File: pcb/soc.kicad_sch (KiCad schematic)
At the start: 1 part, among them U1 XC7Z020CLG484

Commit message: hierarchy and cleaning
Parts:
- removed U1: XC7Z020CLG484, Package_BGA:Xilinx_CLG484_CLG485, symbol library:XC7Z020CLG484
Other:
- added sheet FPGA 0, 13, 33 (soc-1.kicad_sch)
- added sheet FPGA 34, 35 (soc-2.kicad_sch)
- added sheet SoC DDR (soc-ddr.kicad_sch)
- added sheet SoC banks 500, 501 (soc-ps.kicad_sch)
- sheet Power ports: added 1V0_FD, 1V8_FD; removed none

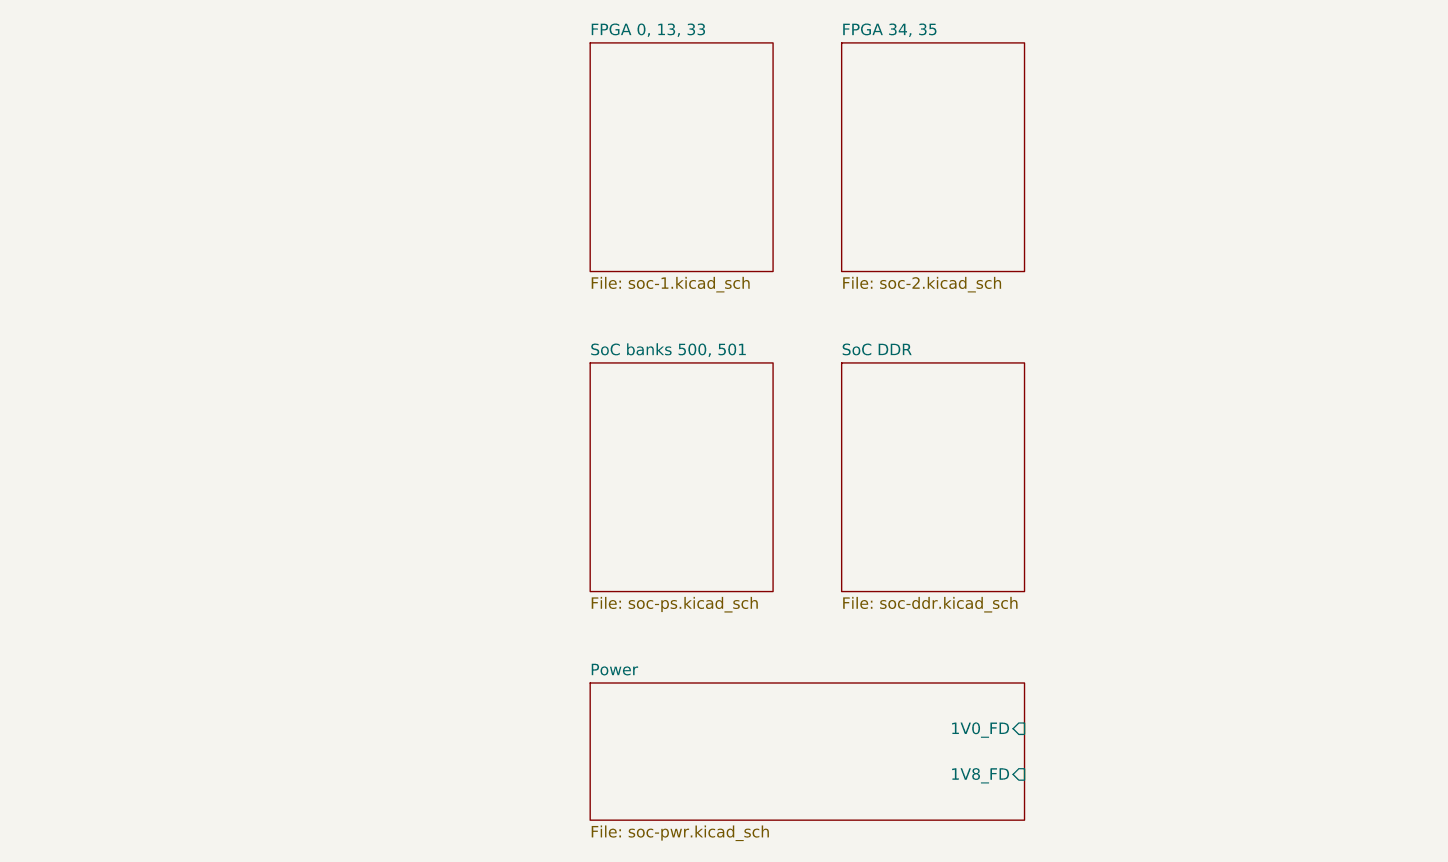
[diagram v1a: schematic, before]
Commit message: schematic structure, added qspi flash, pinout defs. mostly work on PS pinouts, defining comms. buses, still need to choose dram part, phys, camera/bus, power supply etc
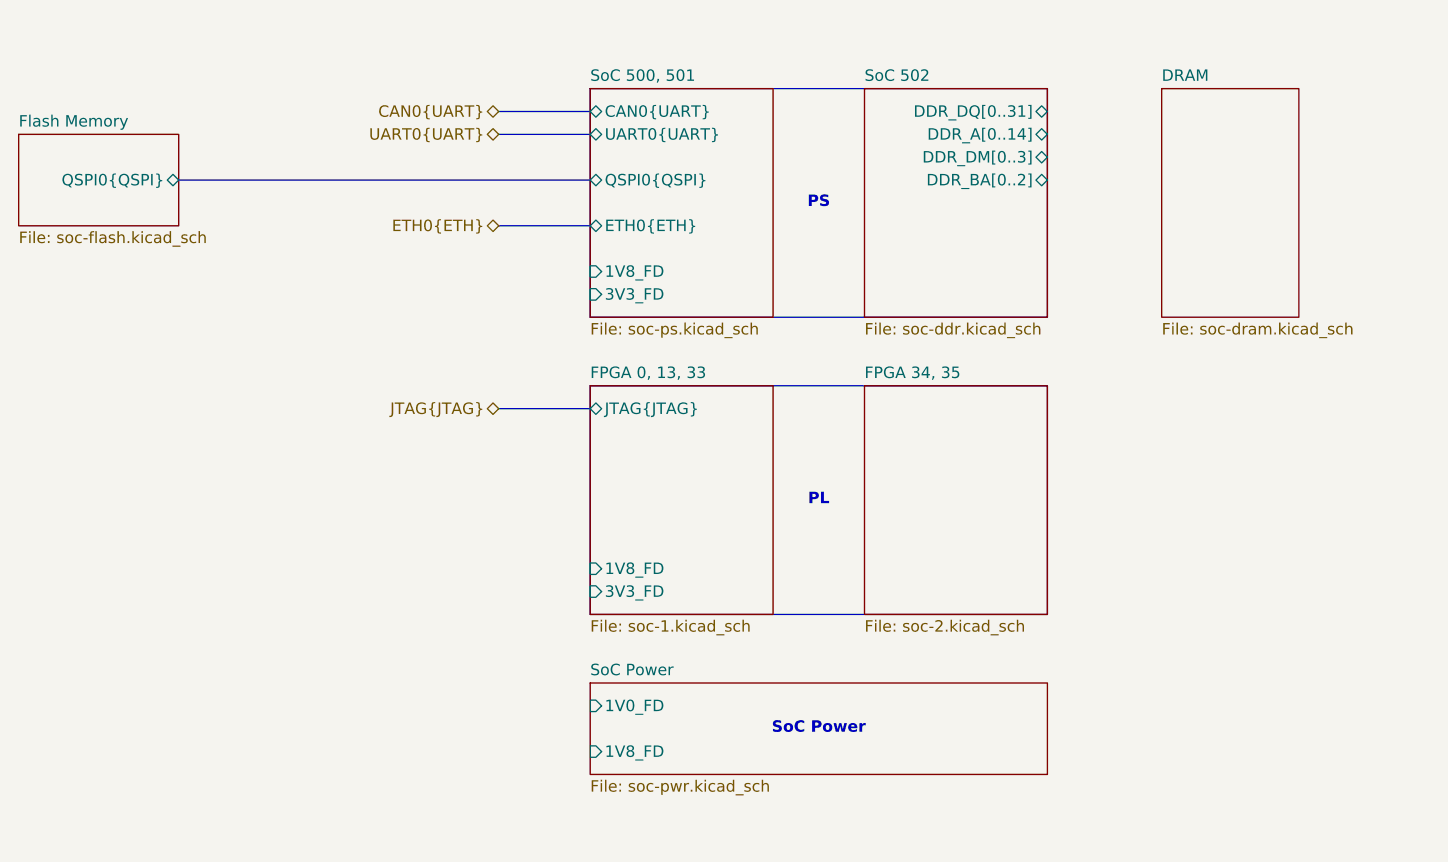
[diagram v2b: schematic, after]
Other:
- sheet Power renamed SoC Power
- sheet SoC DDR renamed SoC 502
- sheet SoC banks 500, 501 renamed SoC 500, 501
- added sheet DRAM (soc-dram.kicad_sch)
- added sheet Flash Memory (soc-flash.kicad_sch)
- sheet FPGA 0, 13, 33 ports: added 1V8_FD, 3V3_FD, JTAG{JTAG}; removed none
- sheet SoC 500, 501 ports: added 1V8_FD, 3V3_FD, CAN0{UART}, ETH0{ETH}, QSPI0{QSPI}, UART0{UART}; removed none
- sheet SoC 502 ports: added DDR_A[0..14], DDR_BA[0..2], DDR_DM[0..3], DDR_DQ[0..31]; removed none
- note added: "PL"
- note added: "PS"
- note added: "SoC Power"
- title: (none) -> CUTIE-CITRUS

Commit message: edits to eth0 protocol names / bus aliases
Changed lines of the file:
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@@
 		)
 	)
-	(hierarchical_label "ETH0{ETH}"
+	(hierarchical_label "ETH0{RGMII}"
 		(shape bidirectional)
 		(at 111.76 76.2 180)

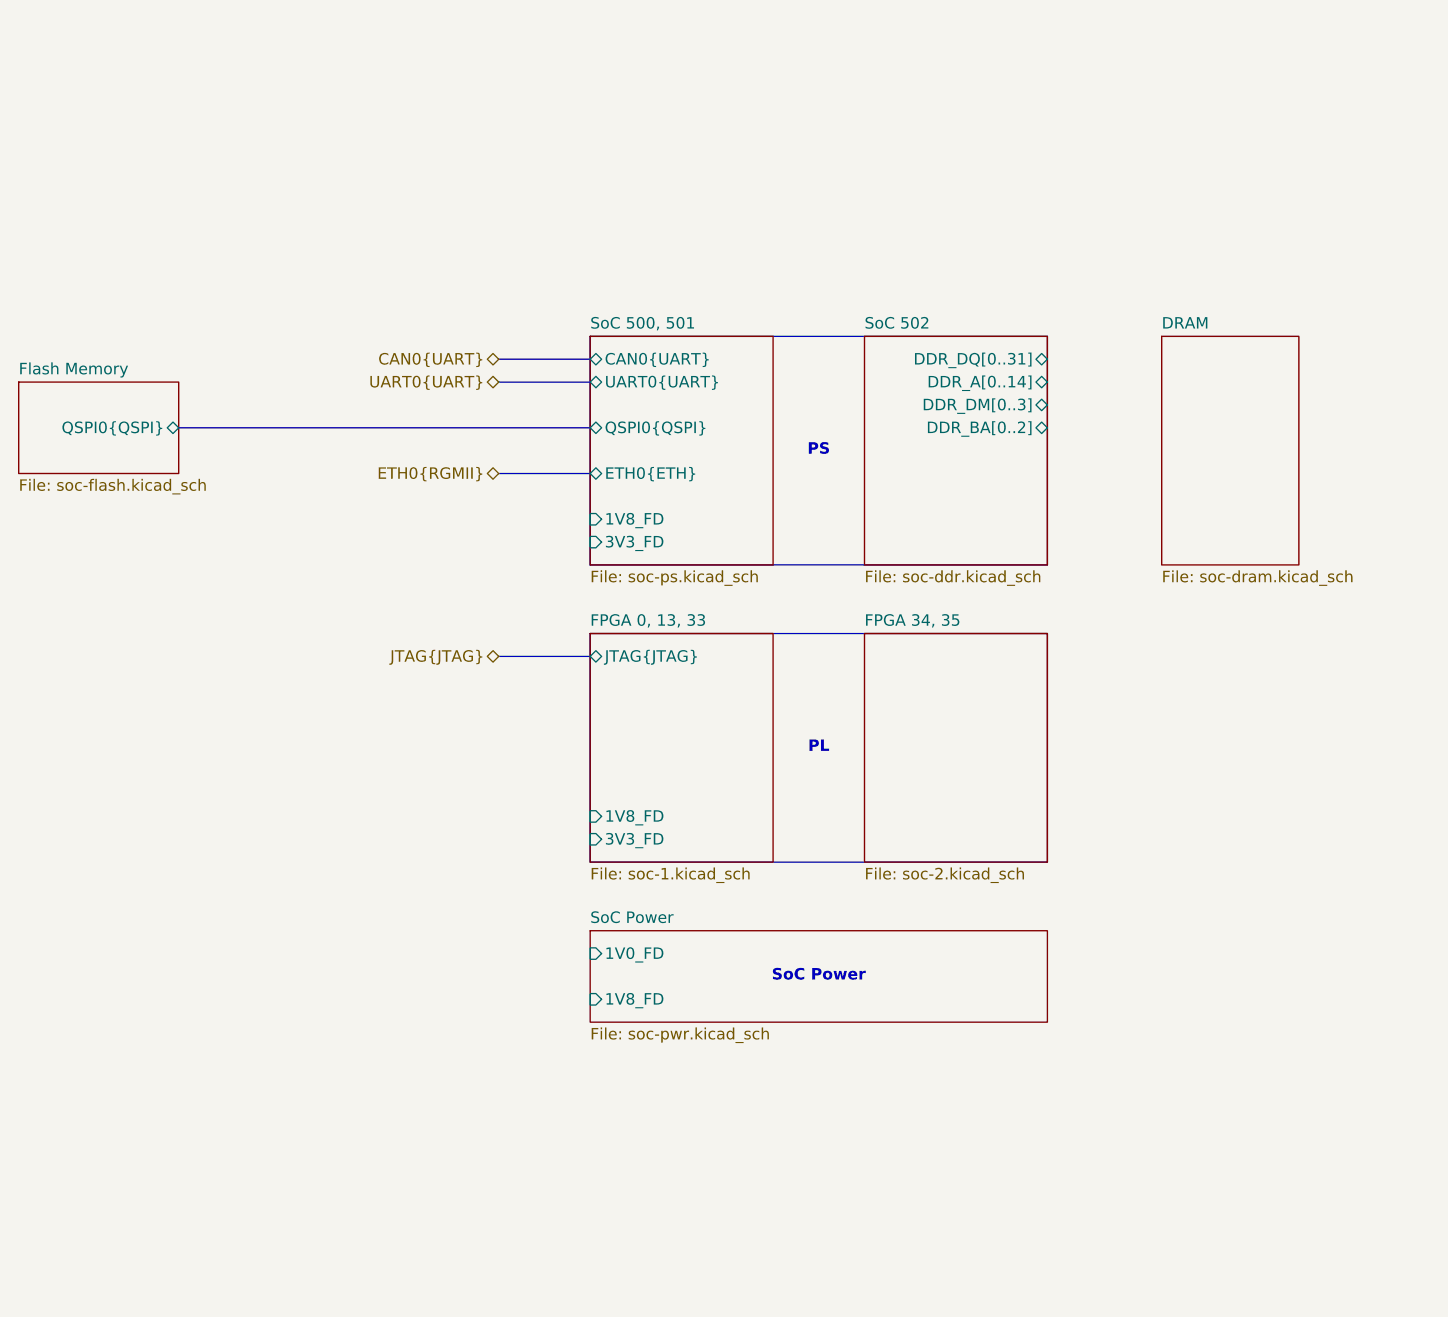
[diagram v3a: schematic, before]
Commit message: added ddr3l
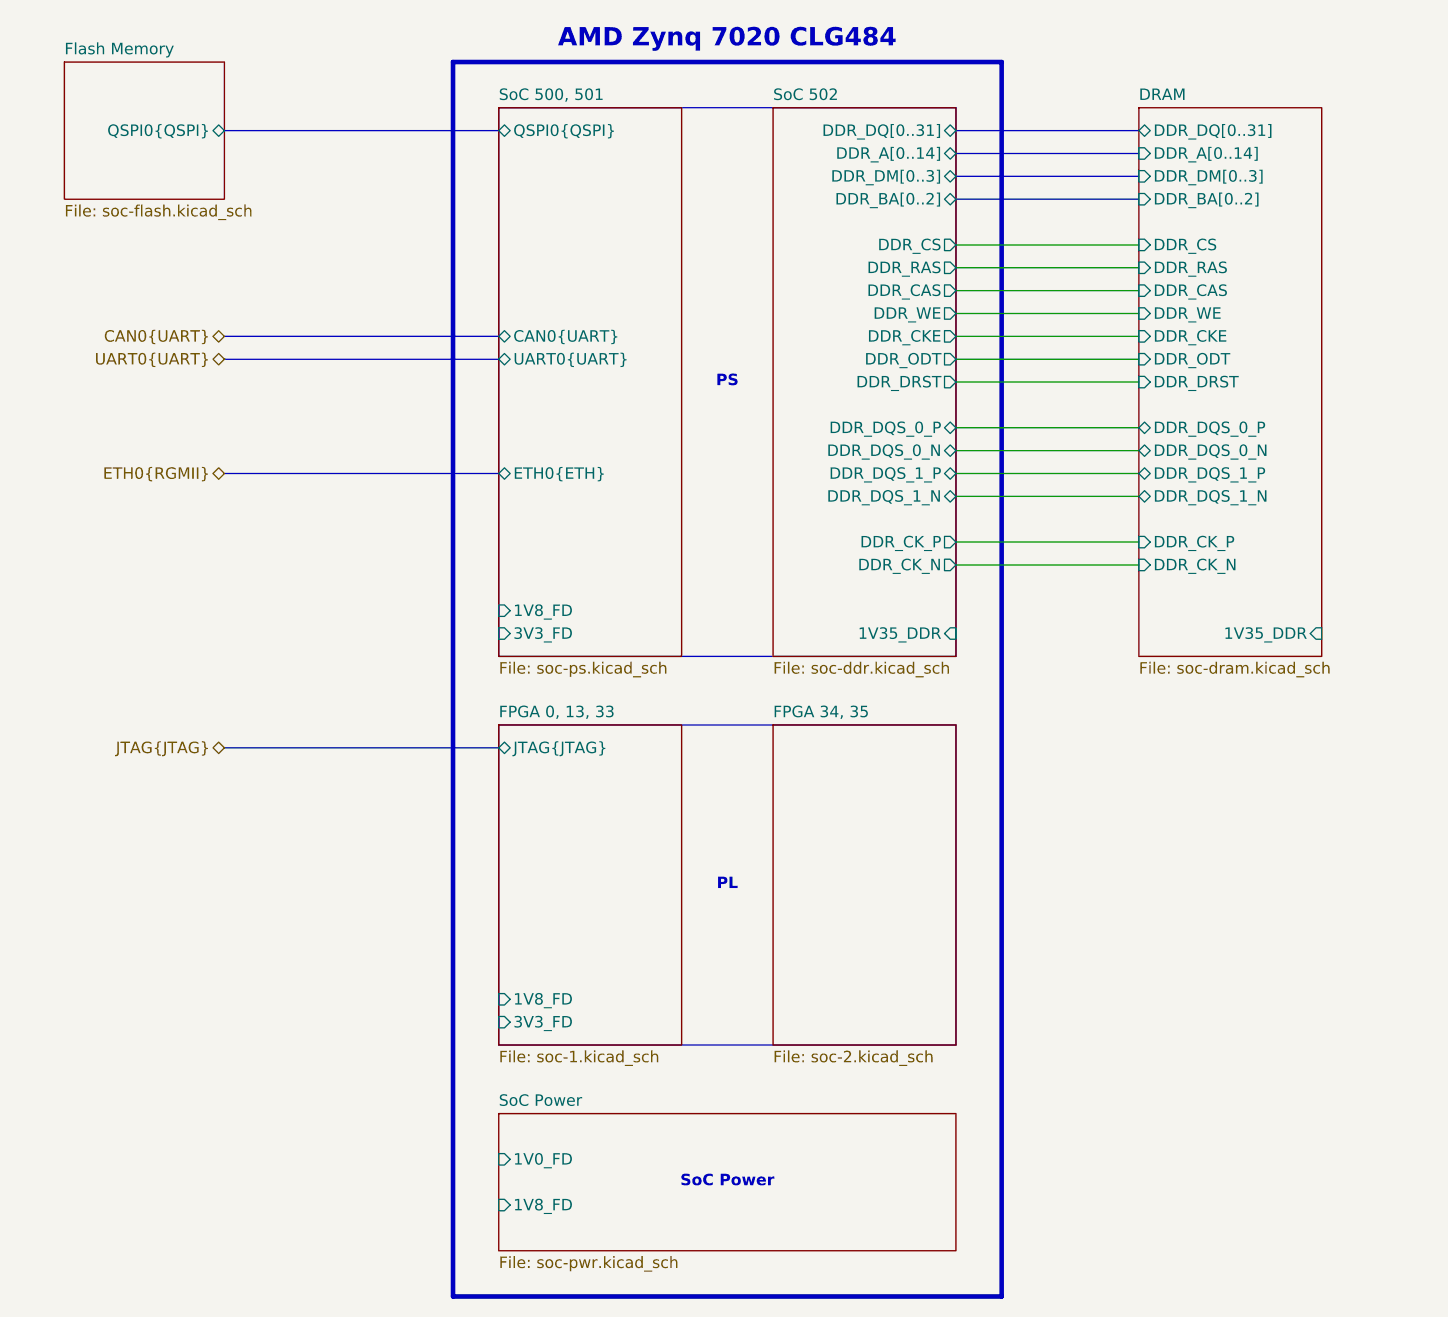
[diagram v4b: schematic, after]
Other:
- sheet DRAM ports: added 1V35_DDR, DDR_A[0..14], DDR_BA[0..2], DDR_CAS, DDR_CKE, DDR_CK_N, DDR_CK_P, DDR_CS, DDR_DM[0..3], DDR_DQS_0_N, DDR_DQS_0_P, DDR_DQS_1_N, DDR_DQS_1_P, DDR_DQ[0..31], DDR_DRST, DDR_ODT, DDR_RAS, DDR_WE; removed none
- sheet SoC 502 ports: added 1V35_DDR, DDR_CAS, DDR_CKE, DDR_CK_N, DDR_CK_P, DDR_CS, DDR_DQS_0_N, DDR_DQS_0_P, DDR_DQS_1_N, DDR_DQS_1_P, DDR_DRST, DDR_ODT, DDR_RAS, DDR_WE; removed none
- note added: "AMD Zynq 7020 CLG484"

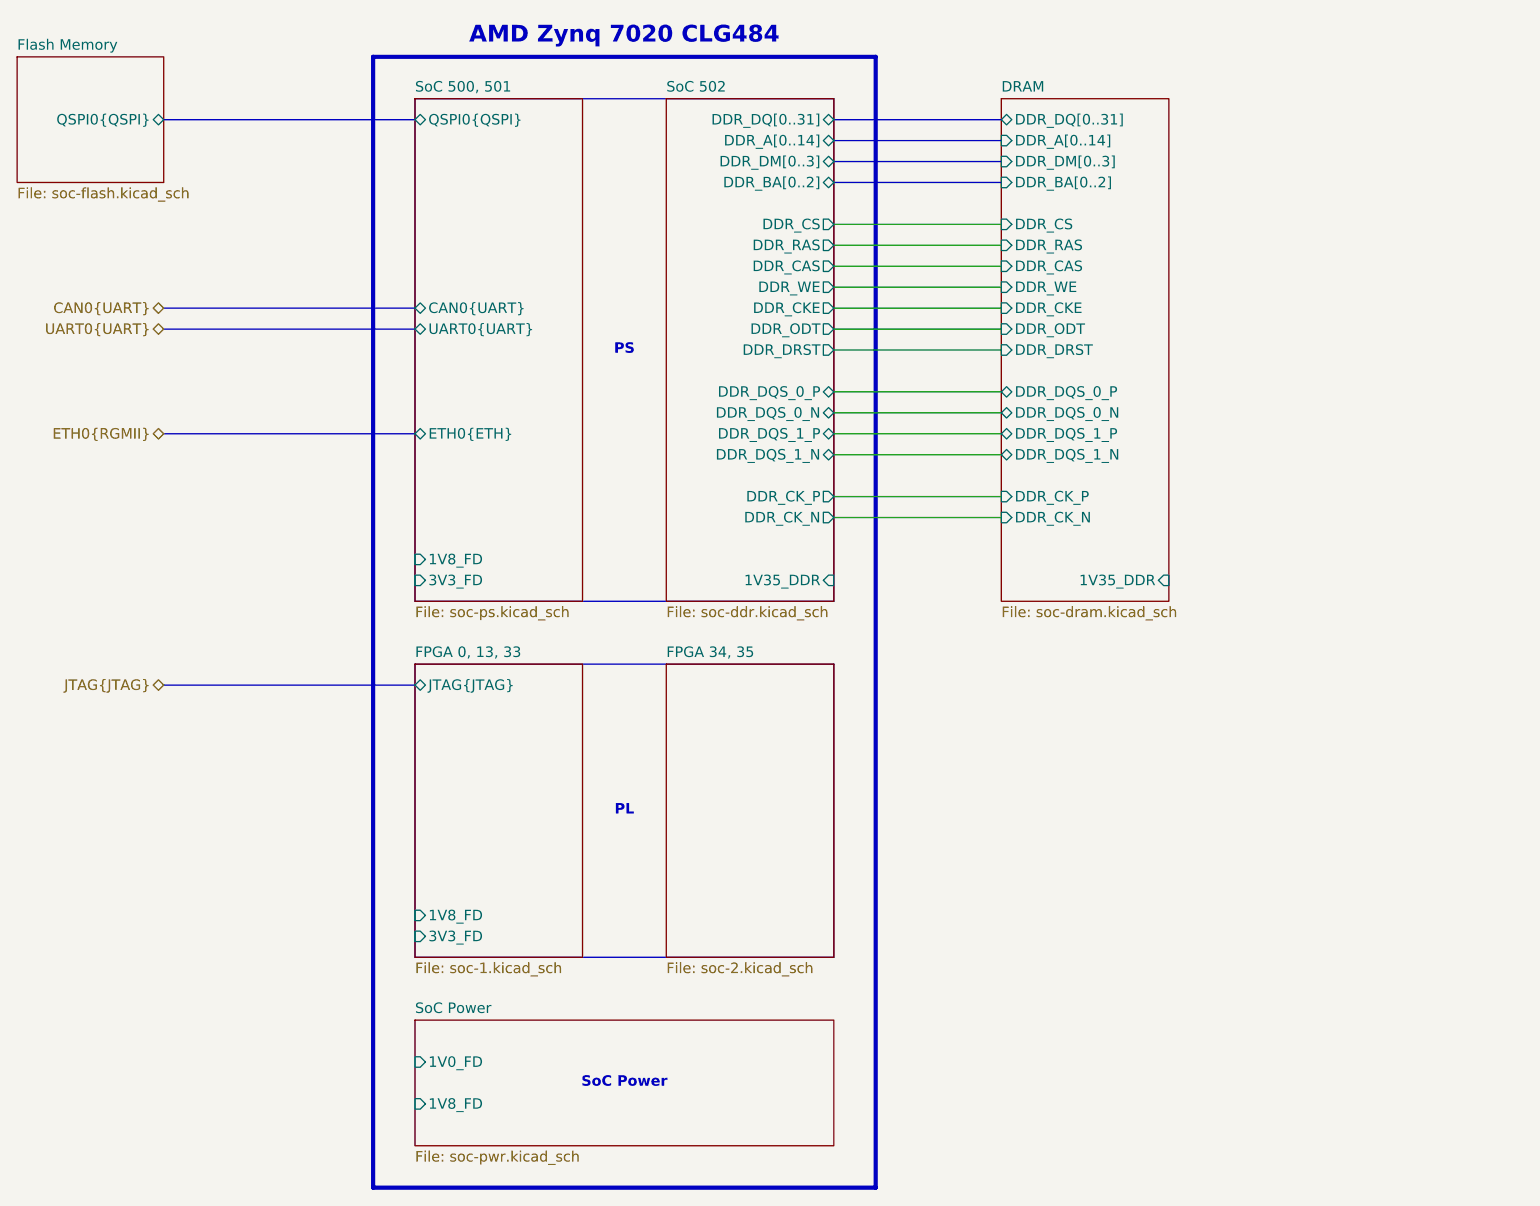
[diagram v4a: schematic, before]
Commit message: add eth phy
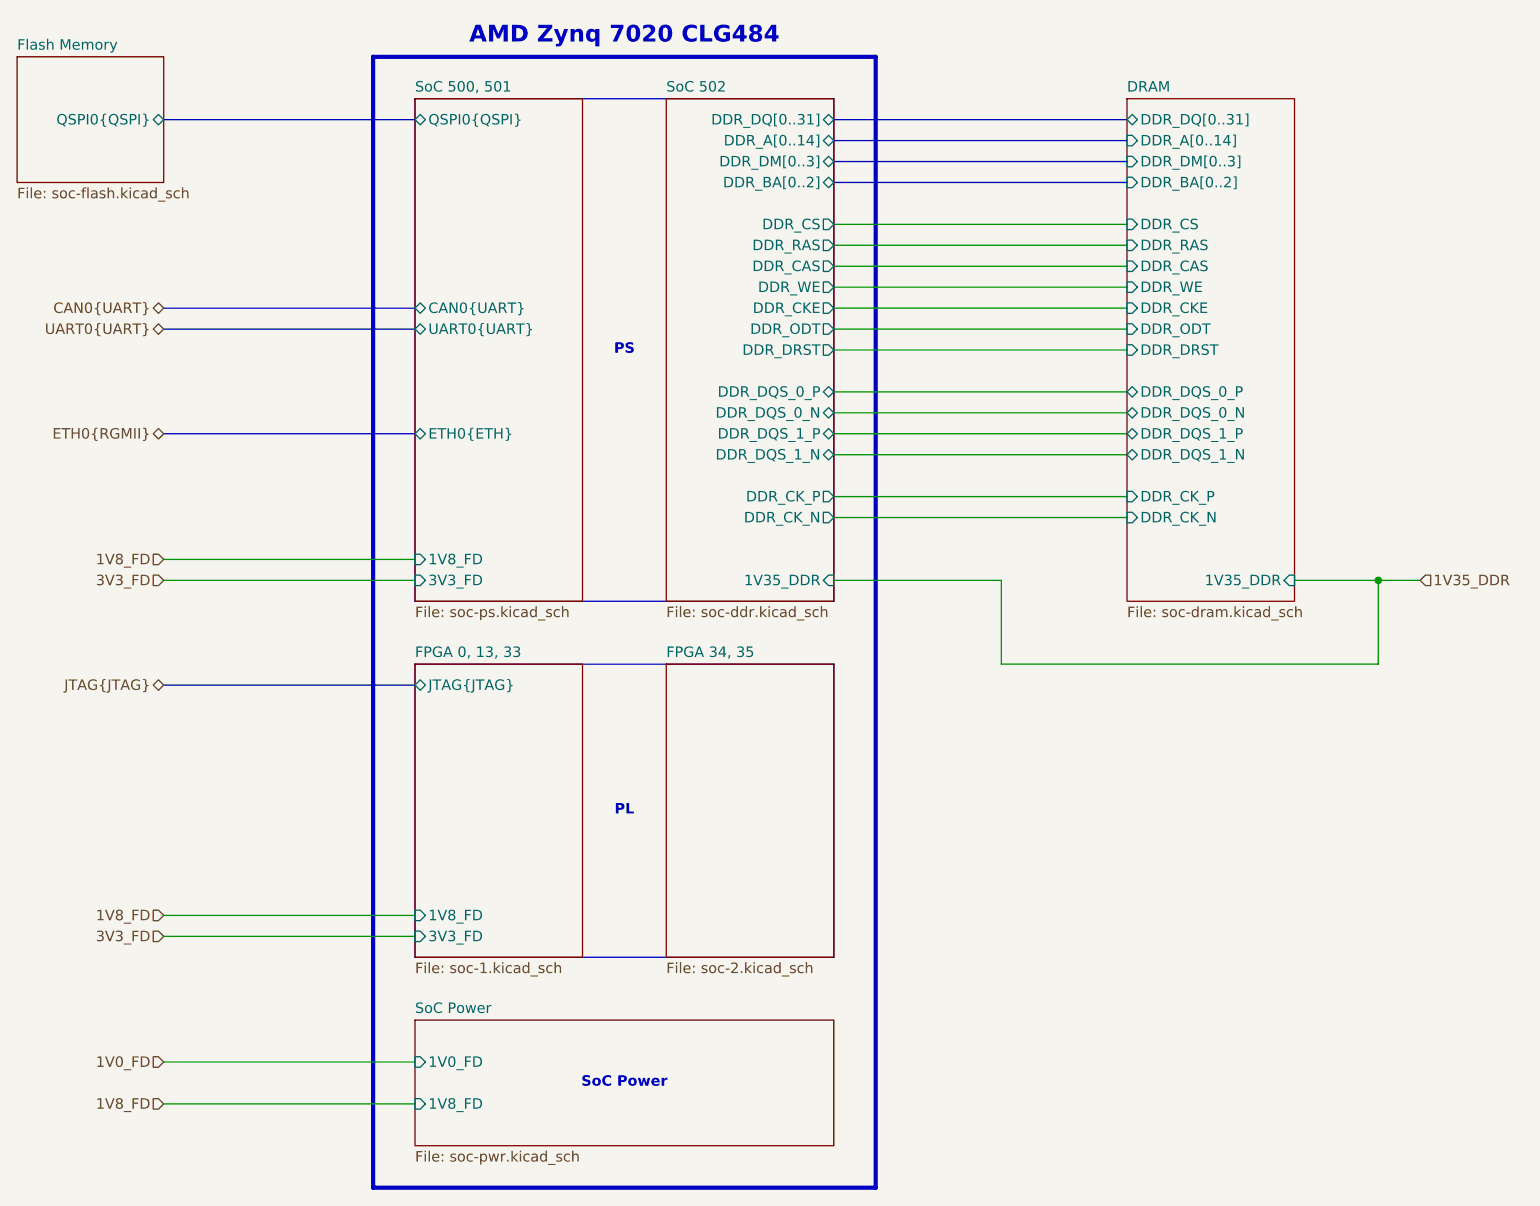
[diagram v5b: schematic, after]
